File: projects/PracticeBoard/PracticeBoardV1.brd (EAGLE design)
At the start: 64 x 64 mm, 51 parts, among them U1 TPS63001, U3 AND, U4 OR

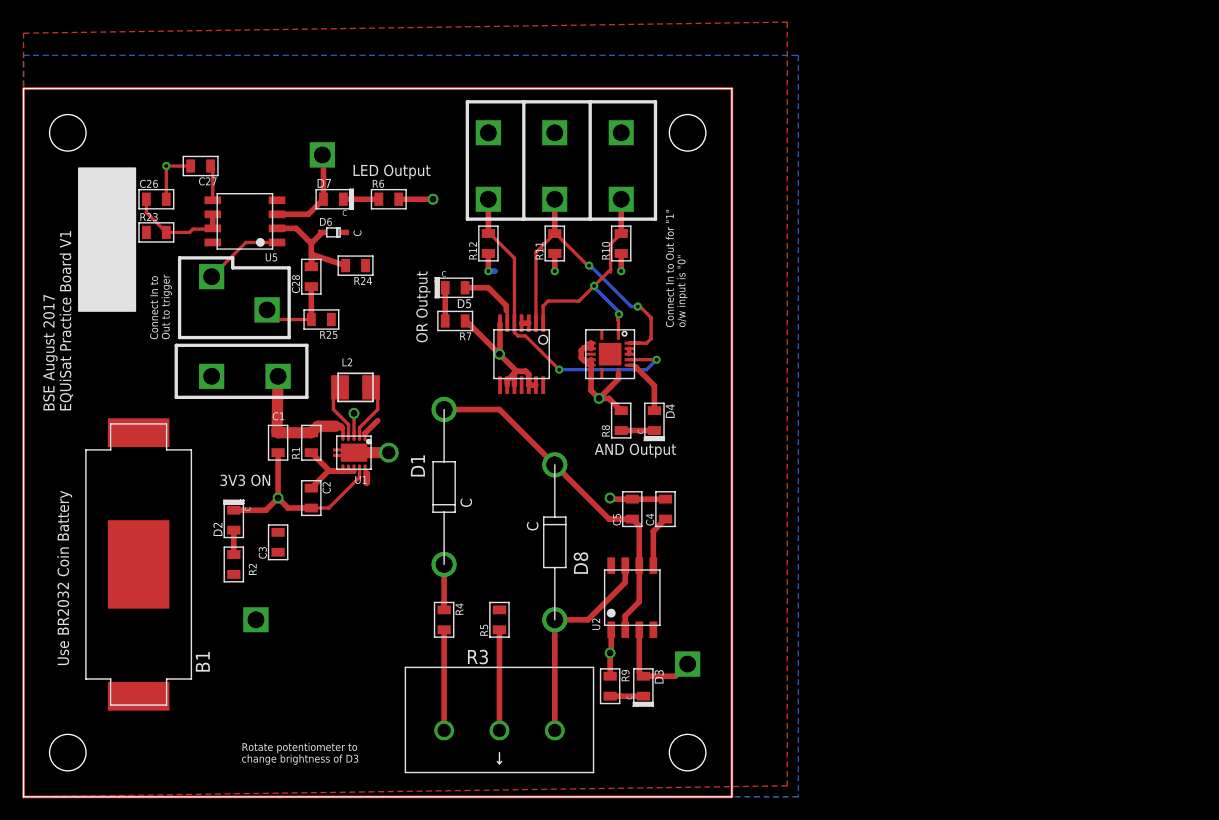
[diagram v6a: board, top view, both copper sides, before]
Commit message: PracticeBoardV1--Added 2 series 2AA batteries--Added pwr supply option--Changed board layout to reflect those additions
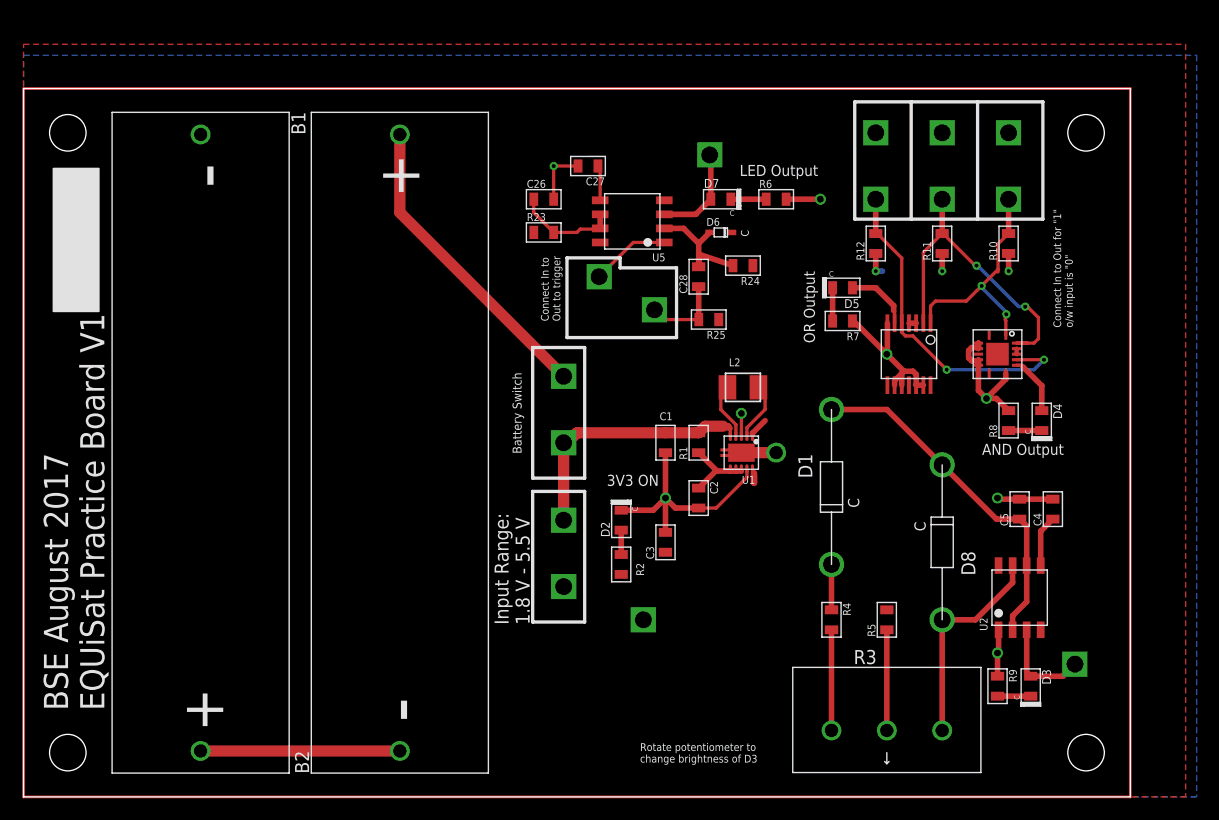
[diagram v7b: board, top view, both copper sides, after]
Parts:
- added B2: 1.5 V, BrownSpaceEngineering:BCAAPC-BATT-HOLDER
- added V14: BATT, BrownSpaceEngineering:VIA-60MIL-SQ
- added V15: INPUT, BrownSpaceEngineering:VIA-60MIL-SQ
- B1: value Use BR2032 - 3V (2V END POINT) -> 1.5 V; device BrownSpaceEngineering:BC-2003-COIN-BATTERY-HOLDER -> BrownSpaceEngineering:BCAAPC-BATT-HOLDER
- V10: value BATT -> PWR-
- V11: value INPUT -> PWR+
- moved V10 37.0 mm to (48.8, 19.0), turned to 90 degrees
- moved C1 35.0 mm to (58.0, 32.0)
- moved C2 35.0 mm to (61.0, 27.0)
- moved C26 35.0 mm to (47.0, 54.0)
- moved C27 35.0 mm to (51.0, 57.0)
- moved C28 35.0 mm to (61.0, 47.0)
- moved C3 35.0 mm to (58.0, 23.0)
- moved C4 35.0 mm to (93.0, 26.0)
- moved C5 35.0 mm to (90.0, 26.0)
- moved D1 35.0 mm to (73.0, 28.0)
- moved D2 35.0 mm to (54.0, 25.0)
- moved D3 35.0 mm to (91.0, 10.0)
- moved D4 35.0 mm to (92.0, 34.0)
- moved D5 35.0 mm to (74.0, 46.0)
- moved D6 35.0 mm to (63.0, 51.0)
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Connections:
- new net N$15: B2.PLUS, V14.P$1
- net GND: now also B1.MINUS, V10.P$1; no longer B1.-
- net N$1: now also B1.PLUS, B2.MINUS; no longer B1.+(1), B1.+(2), V10.P$1
- net VIN: now also V15.P$1
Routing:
- net DIM-WIRE: track 256.0 -> 328.0 mm
- net N$15: track 0.00 -> 28.0 mm
- net N$1: track 0.00 -> 18.0 mm
- net VIN: track 11.9 -> 23.4 mm
- net GND: track 81.8 -> 84.9 mm
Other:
- board size 64 x 64 mm -> 100 x 64 mm
- board text added: "Battery Switch"
- board text added: "Input Range: 1.8 V - 5.5 V"
- board text removed: "Use BR2032 Coin Battery"

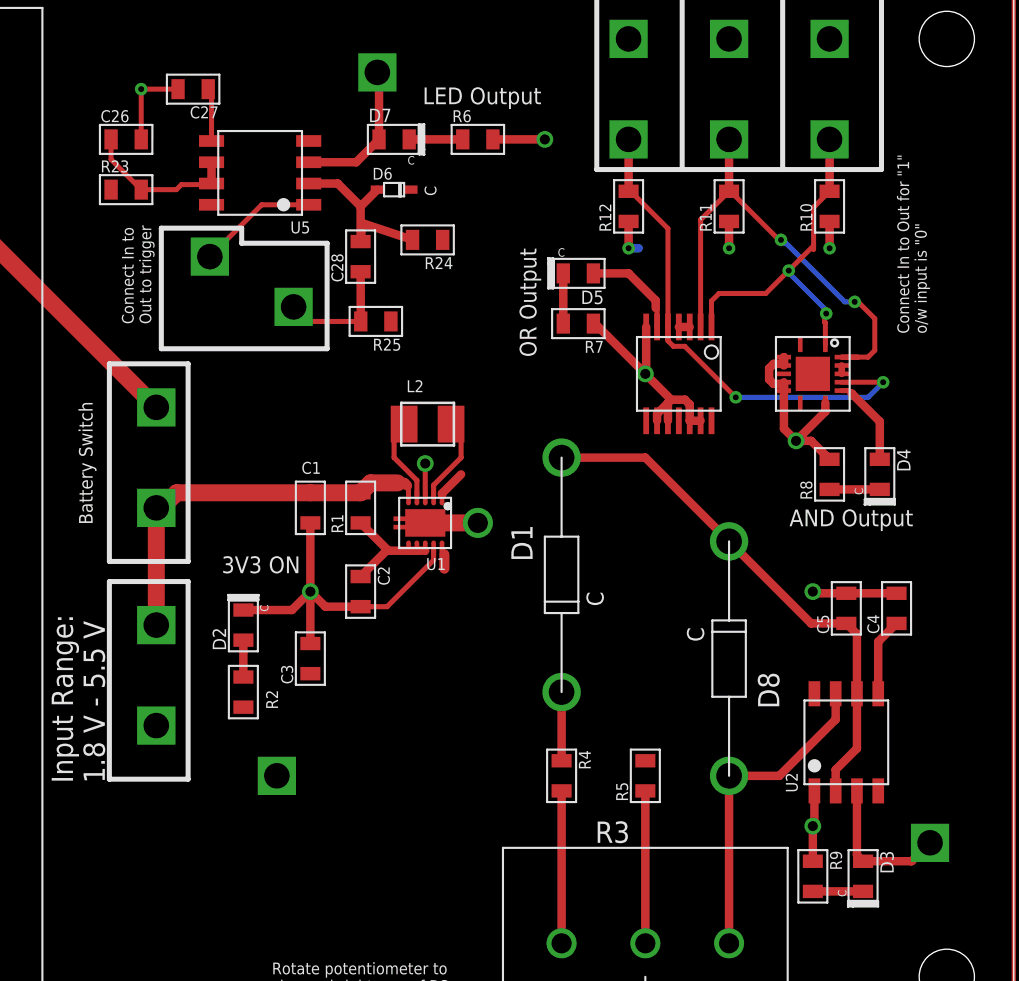
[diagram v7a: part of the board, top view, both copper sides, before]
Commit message: PracticeBoardV1--renumbered parts
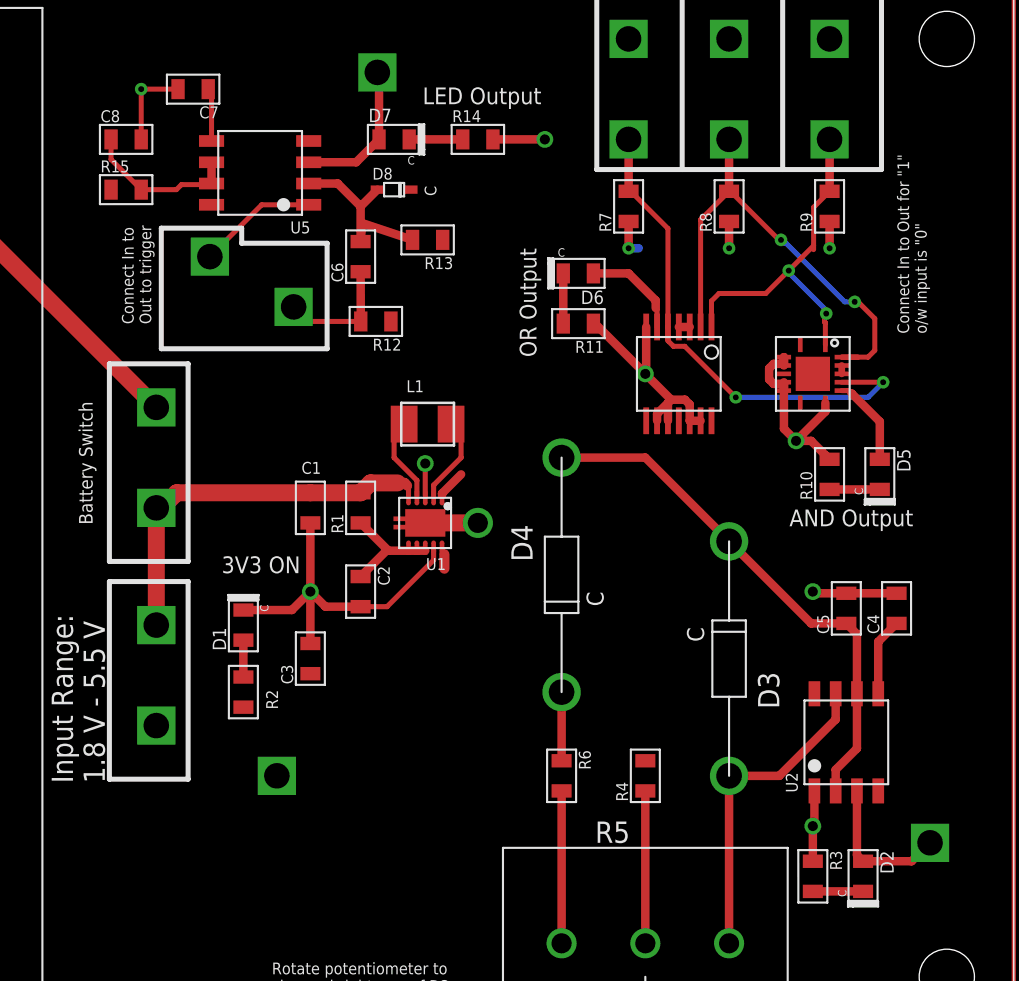
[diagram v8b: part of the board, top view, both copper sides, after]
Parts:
- removed R25: 10K, BrownSpaceEngineering:0805
- added R14: 150R, BrownSpaceEngineering:0805
- D1: value 1N4148THRU-HOLE -> LED0805; device BrownSpaceEngineering:1N4148 -> BrownSpaceEngineering:0805-D
- D3, D4: value LED0805 -> 1N4148THRU-HOLE; device BrownSpaceEngineering:0805-D -> BrownSpaceEngineering:1N4148
- D6: value 1N4148SOD-523FSMD -> LED0805; device BrownSpaceEngineering:SOD-523F -> BrownSpaceEngineering:0805-D
- D8: value 1N4148THRU-HOLE -> 1N4148SOD-523FSMD; device BrownSpaceEngineering:1N4148 -> BrownSpaceEngineering:SOD-523F
- R10, R11: value 10K -> 150R
- R3: value 20K -> 150R; device BrownSpaceEngineering:P160KN -> BrownSpaceEngineering:0805
- R5: value 10K -> 20K; device BrownSpaceEngineering:0805 -> BrownSpaceEngineering:P160KN
- R6, R7, R8, R9: value 150R -> 10K
- V1: value +3V3 -> BATT
- V10: value PWR- -> OUT1
- V11: value PWR+ -> OUT2
- V12: value LED_SHDN -> OUT3
- V13: value ASTABLE_OUT -> IN4
- V14: value BATT -> OUT4
- V15: value INPUT -> LED_SHDN
- V2: value OUT1 -> PWR-
- V3: value IN2 -> INPUT
- V4: value OUT2 -> PWR+
- V5: value IN1 -> +3V3
- V6: value IN3 -> ASTABLE_OUT
- V7: value OUT3 -> IN1
- V8: value IN4 -> IN2
- V9: value OUT4 -> IN3
- moved V13 55.4 mm to (52.0, 47.0), turned to 0 degrees
- moved V5 55.0 mm to (56.0, 16.0), turned to 180 degrees
- moved V10 53.3 mm to (89.0, 54.0), turned to 270 degrees
- moved V2 53.3 mm to (48.8, 19.0), turned to 90 degrees
- moved V6 51.3 mm to (95.0, 12.0)
- moved V11 44.8 mm to (83.0, 54.0), turned to 270 degrees
- moved V4 44.8 mm to (48.8, 25.0), turned to 90 degrees
- moved V3 44.2 mm to (48.8, 32.0), turned to 90 degrees
- moved R9 40.0 mm to (89.0, 50.0), turned to 90 degrees
- moved D2 39.9 mm to (91.0, 10.0), turned to 270 degrees
- moved R6 38.3 mm to (73.0, 16.0), turned to 270 degrees
- moved D8 34.4 mm to (63.0, 51.0), turned to 270 degrees
- moved V8 33.6 mm to (83.0, 60.0), turned to 270 degrees
- moved V15 29.2 mm to (62.0, 58.0), turned to 0 degrees
- moved V9 25.6 mm to (77.0, 60.0), turned to 270 degrees
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- renumbered C26 to C8, C27 to C7, C28 to C6, L2 to L1, R23 to R15, R24 to R13
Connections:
- net !LED_CMD!: now also R12.2, V14.P$1; no longer R25.2, V9.P$1
- net +3V3: now also D8.C, R12.1, R4.2, V7.P$1, V8.P$1, V9.P$1; no longer D6.C, R25.1, R5.2, V1.P$1, V3.P$1, V6.P$1
- net ASTABLE_OUT: now also D2.A, V6.P$1; no longer D3.A, V13.P$1
- net GND: now also D1.C, R10.2, R14.2, R3.1, R8.1, V13.P$1, V2.P$1; no longer D2.C, R10.1, R12.1, R6.2, R8.2, V10.P$1, V8.P$1
- net LED_SHDN: now also V15.P$1; no longer V12.P$1
- net N$10: now also R9.2, V10.P$1; no longer R10.2, V2.P$1
- net N$11: now also R8.2, V11.P$1; no longer R11.2, V4.P$1
- net N$12: now also R7.2, V12.P$1; no longer R12.2, V7.P$1
- net N$15: now also V1.P$1; no longer V14.P$1
- net N$16: now also D3.A, R5.P3; no longer D8.A, R3.P3
- net N$17: now also R5.P1, R6.2; no longer R3.P1, R4.2
- net N$19: now also R14.1; no longer R6.1
- net N$21: now also D5.A; no longer D4.A
- net N$22: now also D2.C, R3.2; no longer D3.C, R9.2
- net N$24: now also D6.A; no longer D5.A
- net N$25: now also D4.C, R6.1; no longer D1.C, R4.1
- net N$3: now also D3.C, D4.A; no longer D1.A, D8.C
- net N$31: now also D1.A; no longer D2.A
- net N$4: now also D5.C, R10.1; no longer D4.C, R8.1
- net N$7: now also R4.1, R5.P2; no longer R3.P2, R5.1
- net N$8: now also D6.C, R11.2; no longer D5.C, R7.2
- net TRIG: now also D8.A; no longer D6.A
- net VIN: now also V3.P$1, V4.P$1; no longer V11.P$1, V15.P$1
